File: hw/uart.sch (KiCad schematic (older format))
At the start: 10 parts

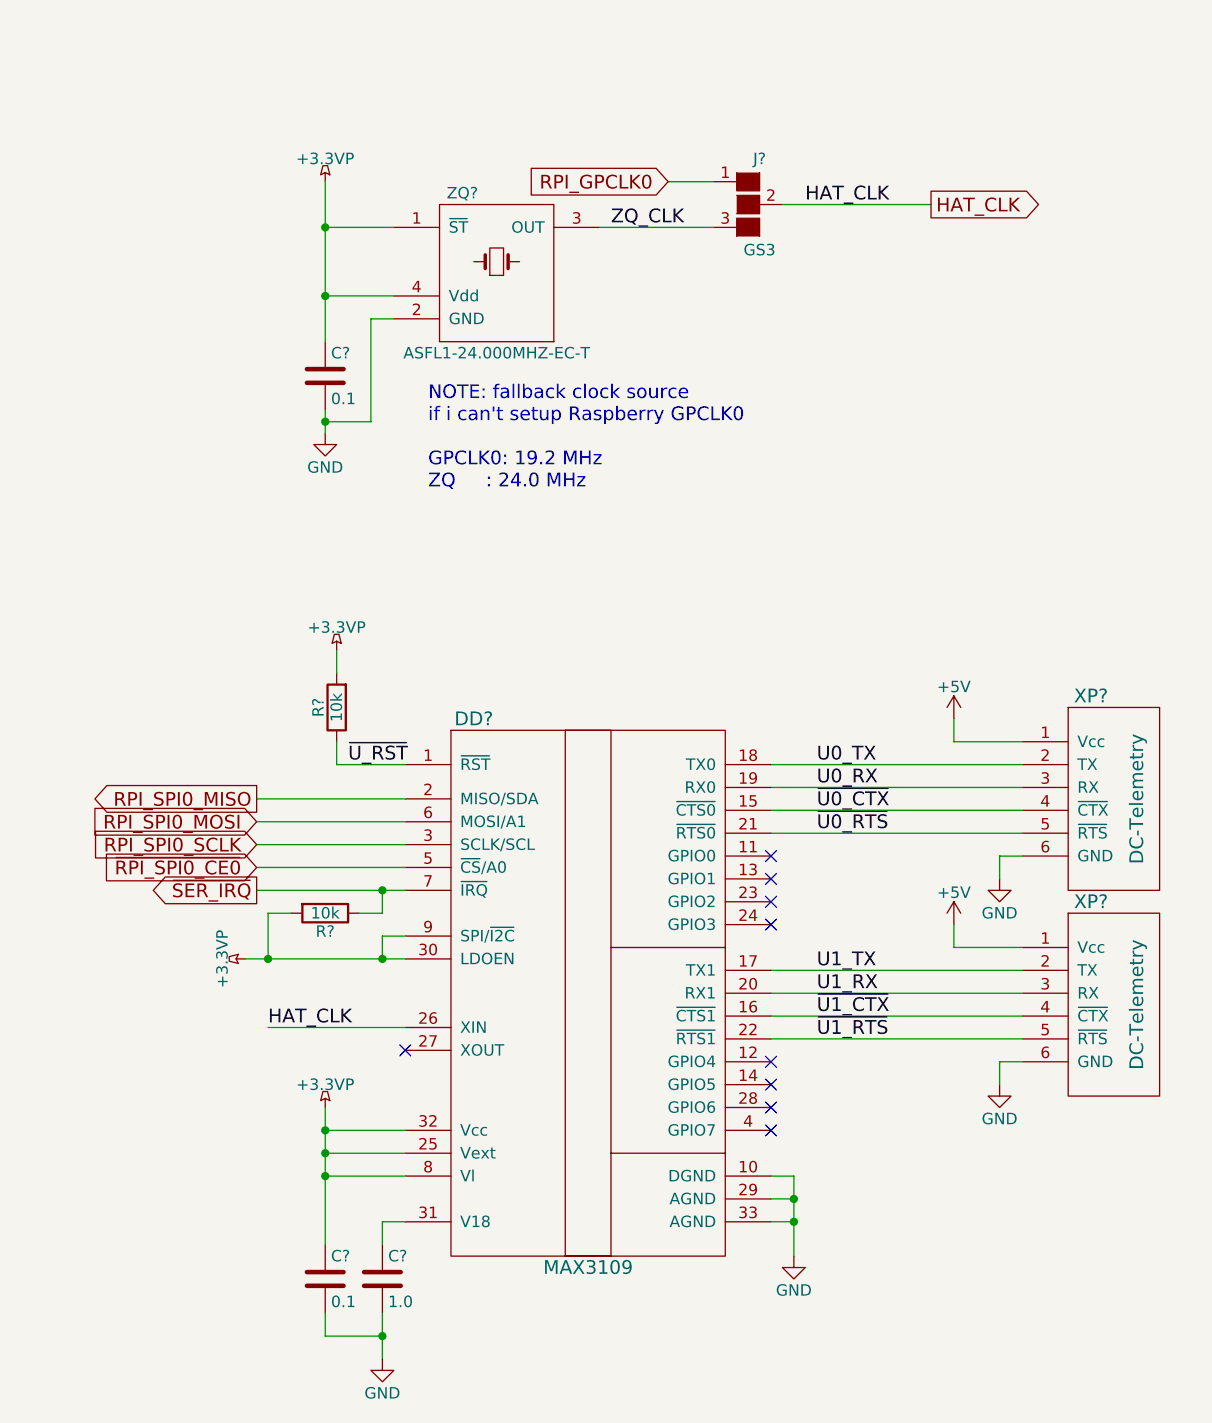
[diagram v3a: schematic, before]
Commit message: hw: add RTC sheet
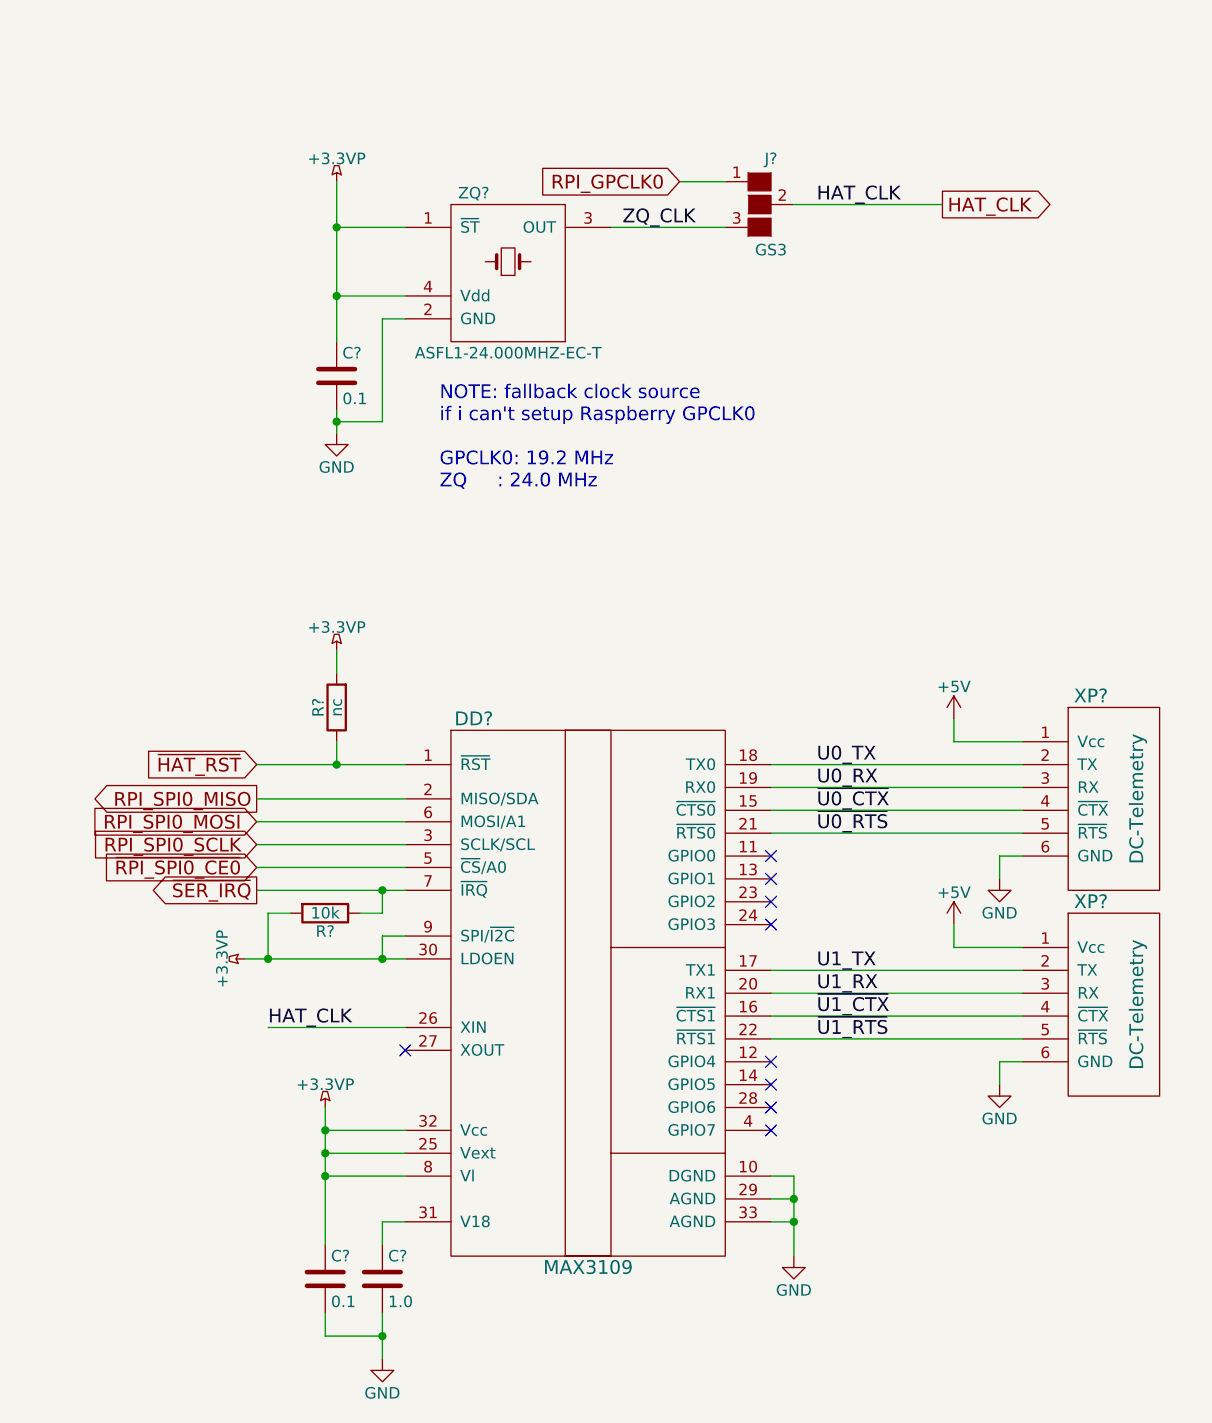
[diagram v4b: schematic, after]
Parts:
- R?: value 10k -> nc
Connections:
- net ~U_RST renamed ~HAT_RST
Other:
- moved on the sheet: C?, J?, ZQ?
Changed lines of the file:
@@
 P 3150 5350
 F 0 "R?" V 3230 5350 50  0000 C CNN
-F 1 "10k" V 3150 5350 50  0000 C CNN
+F 1 "nc" V 3150 5350 50  0000 C CNN
 F 2 "" V 3080 5350 50  0001 C CNN
 F 3 "" H 3150 5350 50  0001 C CNN
@@
 $EndComp
 Wire Wire Line
-	3450 5600 3150 5600
+	2800 5600 3450 5600
 Wire Wire Line
 	3150 5600 3150 5500
@@
 L ASFL1 ZQ?
 U 1 1 5AB33753
-P 3850 3400
-F 0 "ZQ?" H 3700 3700 50  0000 C CNN
-F 1 "ASFL1-24.000MHZ-EC-T" H 3850 3000 50  0000 C CNN
-F 2 "Crystals:Crystal_SMD_Abracon_ABM3B-4pin_5.0x3.2mm" H 3850 3400 50  0001 C CNN
-F 3 "https://www.terraelectronica.ru/pdf/show?pdf_file=%252Fds%252Fpdf%252FA%252FASFL1-24.pdf" H 3850 3400 50  0001 C CNN
-	1    3850 3400
+P 3900 3400
+F 0 "ZQ?" H 3750 3700 50  0000 C CNN
+F 1 "ASFL1-24.000MHZ-EC-T" H 3900 3000 50  0000 C CNN
+F 2 "Crystals:Crystal_SMD_Abracon_ABM3B-4pin_5.0x3.2mm" H 3900 3400 50  0001 C CNN
+F 3 "https://www.terraelectronica.ru/pdf/show?pdf_file=%252Fds%252Fpdf%252FA%252FASFL1-24.pdf" H 3900 3400 50  0001 C CNN
+	1    3900 3400
 	1    0    0    -1
 $EndComp
@@
 L +3.3VP #PWR?
 U 1 1 5AB34755
-P 3100 3050
-F 0 "#PWR?" H 3250 3000 50  0001 C CNN
-F 1 "+3.3VP" H 3100 3150 50  0000 C CNN
-F 2 "" H 3100 3050 50  0001 C CNN
-F 3 "" H 3100 3050 50  0001 C CNN
-	1    3100 3050
+P 3150 3050
+F 0 "#PWR?" H 3300 3000 50  0001 C CNN
+F 1 "+3.3VP" H 3150 3150 50  0000 C CNN
+F 2 "" H 3150 3050 50  0001 C CNN
+F 3 "" H 3150 3050 50  0001 C CNN
+	1    3150 3050
 	1    0    0    -1
 $EndComp
@@
 L C C?
 U 1 1 5AB3478D
-P 3100 3900
-F 0 "C?" H 3125 4000 50  0000 L CNN
-F 1 "0.1" H 3125 3800 50  0000 L CNN
-F 2 "" H 3138 3750 50  0001 C CNN
-F 3 "" H 3100 3900 50  0001 C CNN
-	1    3100 3900
+P 3150 3900
+F 0 "C?" H 3175 4000 50  0000 L CNN
+F 1 "0.1" H 3175 3800 50  0000 L CNN
+F 2 "" H 3188 3750 50  0001 C CNN
+F 3 "" H 3150 3900 50  0001 C CNN
+	1    3150 3900
 	1    0    0    -1
 $EndComp
@@
 L GND #PWR?
 U 1 1 5AB347BB
-P 3100 4150
-F 0 "#PWR?" H 3100 3900 50  0001 C CNN
-F 1 "GND" H 3100 4000 50  0000 C CNN
-F 2 "" H 3100 4150 50  0001 C CNN
-F 3 "" H 3100 4150 50  0001 C CNN
-	1    3100 4150
-	1    0    0    -1
-$EndComp
-Wire Wire Line
-	3100 3550 3400 3550
-Wire Wire Line
-	3100 3050 3100 3750
-Connection ~ 3100 3550
-Wire Wire Line
-	3100 4050 3100 4150
-Wire Wire Line
-	3400 3650 3300 3650
-Wire Wire Line
-	3300 3650 3300 4100
-Wire Wire Line
-	3300 4100 3100 4100
-Connection ~ 3100 4100
-Wire Wire Line
-	3400 3250 3100 3250
-Connection ~ 3100 3250
+P 3150 4150
+F 0 "#PWR?" H 3150 3900 50  0001 C CNN
+F 1 "GND" H 3150 4000 50  0000 C CNN
+F 2 "" H 3150 4150 50  0001 C CNN
+F 3 "" H 3150 4150 50  0001 C CNN
+	1    3150 4150
+	1    0    0    -1
+$EndComp
+Wire Wire Line
+	3150 3550 3450 3550
+Wire Wire Line
+	3150 3050 3150 3750
+Connection ~ 3150 3550
+Wire Wire Line
+	3150 4050 3150 4150
+Wire Wire Line
+	3450 3650 3350 3650
+Wire Wire Line
+	3350 3650 3350 4100
+Wire Wire Line
+	3350 4100 3150 4100
+Connection ~ 3150 4100
+Wire Wire Line
+	3450 3250 3150 3250
+Connection ~ 3150 3250
 $Comp
 L GS3 J?
 U 1 1 5AB34FDF
-P 4950 3150
-F 0 "J?" H 5000 3350 50  0000 C CNN
-F 1 "GS3" H 5000 2951 50  0000 C CNN
-F 2 "Connectors:GS3" V 5038 3076 50  0001 C CNN
-F 3 "" H 4950 3150 50  0001 C CNN
-	1    4950 3150
-	1    0    0    -1
-$EndComp
-Text GLabel 4600 3050 0    60   Input ~ 0
+P 5000 3150
+F 0 "J?" H 5050 3350 50  0000 C CNN
+F 1 "GS3" H 5050 2951 50  0000 C CNN
+F 2 "Connectors:GS3" V 5088 3076 50  0001 C CNN
+F 3 "" H 5000 3150 50  0001 C CNN
+	1    5000 3150
+	1    0    0    -1
+$EndComp
+Text GLabel 4650 3050 0    60   Input ~ 0
 RPI_GPCLK0
 Wire Wire Line
-	4800 3250 4300 3250
-Wire Wire Line
-	4600 3050 4800 3050
-Text Label 4350 3250 0    60   ~ 0
+	4850 3250 4350 3250
+Wire Wire Line
+	4650 3050 4850 3050
+Text Label 4400 3250 0    60   ~ 0
 ZQ_CLK
-Text GLabel 5750 3150 2    60   Output ~ 0
+Text GLabel 5800 3150 2    60   Output ~ 0
 HAT_CLK
 Wire Wire Line
-	5100 3150 5750 3150
-Text Label 5200 3150 0    60   ~ 0
+	5150 3150 5800 3150
+Text Label 5250 3150 0    60   ~ 0
 HAT_CLK
-Text Notes 3550 4400 0    60   ~ 0
+Text Notes 3600 4400 0    60   ~ 0
 NOTE: fallback clock source\nif i can't setup Raspberry GPCLK0\n\nGPCLK0: 19.2 MHz\nZQ     : 24.0 MHz
-Text Label 3200 5600 0    60   ~ 0
-~U_RST
 Wire Wire Line
 	3450 6750 2850 6750
@@
 NoConn ~ 5050 7100
 NoConn ~ 5050 7200
+Text GLabel 2800 5600 0    60   Input ~ 0
+~HAT_RST
+Connection ~ 3150 5600
 $EndSCHEMATC

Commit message: switch to KiCAD 5 (nightly)
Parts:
- removed C?: 0.1, symbol C
- removed C?: 1.0, symbol C
- removed J?: GS3, Connectors:GS3, symbol GS3
- added C? (x2): 0.1, symbol Device:C
- added JP?: Jumper_3_Open, symbol Jumper:Jumper_3_Open
- C?: symbol C -> Device:C
- DD?: symbol MAX3109 -> ic:MAX3109
- R? (x2): symbol R -> Device:R
- XP? (x2): symbol DC-Telemetry -> dronecode_con:DC-Telemetry
- ZQ?: symbol ASFL1 -> ic:ASFL1
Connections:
- net +3.3VP: now also C?.1
- net GND: now also C?.2, C?.2
- net HAT_CLK: now also JP?.2 (C)
- net RPI_GPCLK0: now also JP?.3 (B)
- net ZQ_CLK: now also JP?.1 (A)
- net at DD?.31 (V18): now also C?.1
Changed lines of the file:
@@
-EESchema Schematic File Version 2
-LIBS:power
-LIBS:device
-LIBS:transistors
-LIBS:conn
-LIBS:linear
-LIBS:regul
-LIBS:74xx
-LIBS:cmos4000
-LIBS:adc-dac
-LIBS:memory
-LIBS:xilinx
-LIBS:microcontrollers
-LIBS:dsp
-LIBS:microchip
-LIBS:analog_switches
-LIBS:motorola
-LIBS:texas
-LIBS:intel
-LIBS:audio
-LIBS:interface
-LIBS:digital-audio
-LIBS:philips
-LIBS:display
-LIBS:cypress
-LIBS:siliconi
-LIBS:opto
-LIBS:atmel
-LIBS:contrib
-LIBS:valves
-LIBS:rpi_con
-LIBS:ic
-LIBS:dronecode_con
+EESchema Schematic File Version 4
 LIBS:obc-drone-hat-cache
-EELAYER 25 0
+EELAYER 26 0
 EELAYER END
 $Descr A4 8268 11693 portrait
@@
 $EndDescr
 $Comp
-L MAX3109 DD?
+L ic:MAX3109 DD?
 U 1 1 5AB1B0A7
 P 4250 6600
@@
 $EndComp
 $Comp
-L +3.3VP #PWR013
+L power:+3.3VP #PWR013
 U 1 1 5AB1B260
 P 3100 7100
@@
 $EndComp
 $Comp
-L GND #PWR014
+L power:GND #PWR014
 U 1 1 5AB1B2D7
 P 3350 8200
@@
 $EndComp
 NoConn ~ 3450 6850
-$Comp
-L C C?
-U 1 1 5AB1B470
-P 3100 7850
-F 0 "C?" H 3125 7950 50  0000 L CNN
-F 1 "0.1" H 3125 7750 50  0000 L CNN
-F 2 "" H 3138 7700 50  0001 C CNN
-F 3 "" H 3100 7850 50  0001 C CNN
-	1    3100 7850
-	1    0    0    -1
-$EndComp
-$Comp
-L C C?
-U 1 1 5AB1B4D8
-P 3350 7850
-F 0 "C?" H 3375 7950 50  0000 L CNN
-F 1 "1.0" H 3375 7750 50  0000 L CNN
-F 2 "" H 3388 7700 50  0001 C CNN
-F 3 "" H 3350 7850 50  0001 C CNN
-	1    3350 7850
-	1    0    0    -1
-$EndComp
 Wire Wire Line
 	3450 7600 3350 7600
@@
 	3450 7200 3100 7200
 Wire Wire Line
-	3100 7100 3100 7700
+	3100 7100 3100 7200
 Wire Wire Line
 	3100 7300 3450 7300
@@
 Connection ~ 3100 7200
 Wire Wire Line
-	3350 8000 3350 8200
+	3350 8000 3350 8100
 Wire Wire Line
 	3350 8100 3100 8100
@@
 Connection ~ 3350 8100
 $Comp
-L +3.3VP #PWR015
+L power:+3.3VP #PWR015
 U 1 1 5AB1B914
 P 2750 6450
@@
 $EndComp
 $Comp
-L R R?
+L Device:R R?
 U 1 1 5AB1B9A3
 P 3100 6250
@@
 $EndComp
 Wire Wire Line
-	2750 6450 3450 6450
+	2750 6450 2850 6450
 Wire Wire Line
 	3450 6350 3350 6350
@@
 	3450 6050 2800 6050
 Wire Wire Line
-	2800 6150 3450 6150
+	2800 6150 3350 6150
 Wire Wire Line
 	3250 6250 3350 6250
@@
 Connection ~ 3350 6150
 $Comp
-L GND #PWR016
+L power:GND #PWR016
 U 1 1 5AB1C686
 P 6050 6100
@@
 	5050 7400 5150 7400
 Wire Wire Line
-	5150 7400 5150 7750
+	5150 7400 5150 7500
 Wire Wire Line
 	5050 7500 5150 7500
@@
 Connection ~ 5150 7600
 $Comp
-L R R?
+L Device:R R?
 U 1 1 5AB1D90A
 P 3150 5350
@@
 $EndComp
 $Comp
-L +3.3VP #PWR017
+L power:+3.3VP #PWR017
 U 1 1 5AB1D959
 P 3150 5100
@@
 $EndComp
 Wire Wire Line
-	2800 5600 3450 5600
+	2800 5600 3150 5600
 Wire Wire Line
 	3150 5600 3150 5500
@@
 	3150 5200 3150 5100
 $Comp
-L DC-Telemetry XP?
+L dronecode_con:DC-Telemetry XP?
 U 1 1 5AB2FA79
 P 6550 5750
@@
 $EndComp
 $Comp
-L DC-Telemetry XP?
+L dronecode_con:DC-Telemetry XP?
 U 1 1 5AB2FFF0
 P 6550 6650
@@
 	6150 6800 5050 6800
 $Comp
-L +5V #PWR?
+L power:+5V #PWR?
 U 1 1 5AB3063A
 P 5850 5400
@@
 	6050 6000 6050 6100
 $Comp
-L GND #PWR?
+L power:GND #PWR?
 U 1 1 5AB30BD8
 P 5150 7750
@@
 $EndComp
 $Comp
-L GND #PWR?
+L power:GND #PWR?
 U 1 1 5AB30BF8
 P 6050 7000
@@
 $EndComp
 $Comp
-L +5V #PWR?
+L power:+5V #PWR?
 U 1 1 5AB30E1E
 P 5850 6300
@@
 ~U1_RTS
 $Comp
-L ASFL1 ZQ?
+L ic:ASFL1 ZQ?
 U 1 1 5AB33753
 P 3900 3400
@@
 $EndComp
 $Comp
-L +3.3VP #PWR?
+L power:+3.3VP #PWR?
 U 1 1 5AB34755
 P 3150 3050
@@
 $EndComp
 $Comp
-L C C?
+L Device:C C?
 U 1 1 5AB3478D
 P 3150 3900
@@
 $EndComp
 $Comp
-L GND #PWR?
+L power:GND #PWR?
 U 1 1 5AB347BB
 P 3150 4150
@@
 	3150 3550 3450 3550
 Wire Wire Line
-	3150 3050 3150 3750
+	3150 3050 3150 3250
 Connection ~ 3150 3550
 Wire Wire Line
-	3150 4050 3150 4150
+	3150 4050 3150 4100
 Wire Wire Line
 	3450 3650 3350 3650
@@
 	3450 3250 3150 3250
 Connection ~ 3150 3250
-$Comp
-L GS3 J?
-U 1 1 5AB34FDF
-P 5000 3150
-F 0 "J?" H 5050 3350 50  0000 C CNN
-F 1 "GS3" H 5050 2951 50  0000 C CNN
-F 2 "Connectors:GS3" V 5088 3076 50  0001 C CNN
-F 3 "" H 5000 3150 50  0001 C CNN
-	1    5000 3150
-	1    0    0    -1
-$EndComp
-Text GLabel 4650 3050 0    60   Input ~ 0
+Text GLabel 4800 2400 0    60   Input ~ 0
 RPI_GPCLK0
 Wire Wire Line
-	4850 3250 4350 3250
-Wire Wire Line
-	4650 3050 4850 3050
+	5200 3250 4350 3250
+Wire Wire Line
+	4800 2400 5200 2400
 Text Label 4400 3250 0    60   ~ 0
 ZQ_CLK
-Text GLabel 5800 3150 2    60   Output ~ 0
+Text GLabel 5950 2800 2    60   Output ~ 0
 HAT_CLK
 Wire Wire Line
-	5150 3150 5800 3150
-Text Label 5250 3150 0    60   ~ 0
+	5350 2800 5950 2800
+Text Label 5400 2800 0    60   ~ 0
 HAT_CLK
 Text Notes 3600 4400 0    60   ~ 0
@@
 ~HAT_RST
 Connection ~ 3150 5600
+Wire Wire Line
+	3100 7300 3100 7400
+Wire Wire Line
+	3100 7400 3100 7700
+Wire Wire Line
+	3100 7200 3100 7300
+Wire Wire Line
+	3350 8100 3350 8200
+Wire Wire Line
+	3350 6450 3450 6450
+Wire Wire Line
+	2850 6450 3350 6450
+Wire Wire Line
+	3350 6150 3450 6150
+Wire Wire Line
+	5150 7500 5150 7600
+Wire Wire Line
+	5150 7600 5150 7750
+Wire Wire Line
+	3150 3550 3150 3750
+Wire Wire Line
+	3150 4100 3150 4150
+Wire Wire Line
+	3150 3250 3150 3550
+Wire Wire Line
+	3150 5600 3450 5600
+$Comp
+L Jumper:Jumper_3_Open JP?
+U 1 1 5AB6CF92
+P 5200 2800
+F 0 "JP?" V 5246 2886 50  0000 L CNN
+F 1 "Jumper_3_Open" V 5155 2886 50  0000 L CNN
+F 2 "" H 5200 2800 50  0001 C CNN
+F 3 "~" H 5200 2800 50  0001 C CNN
+	1    5200 2800
+	0    -1   -1   0
+$EndComp
+Wire Wire Line
+	5200 2400 5200 2550
+Wire Wire Line
+	5200 3250 5200 3050
+$Comp
+L Device:C C?
+U 1 1 5AC0F665
+P 3100 7850
+F 0 "C?" H 2700 8050 50  0000 L CNN
+F 1 "0.1" H 2850 8050 50  0000 L CNN
+F 2 "" H 3138 7700 50  0001 C CNN
+F 3 "~" H 3100 7850 50  0001 C CNN
+	1    3100 7850
+	1    0    0    -1
+$EndComp
+$Comp
+L Device:C C?
+U 1 1 5AC0F72E
+P 3350 7850
+F 0 "C?" H 2700 7950 50  0000 L CNN
+F 1 "0.1" H 2850 7950 50  0000 L CNN
+F 2 "" H 3388 7700 50  0001 C CNN
+F 3 "~" H 3350 7850 50  0001 C CNN
+	1    3350 7850
+	1    0    0    -1
+$EndComp
 $EndSCHEMATC

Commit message: hw: start stm page
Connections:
- net +3.3VP renamed +3V3
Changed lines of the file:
@@
-$EndComp
-$Comp
-L power:+3.3VP #PWR013
-U 1 1 5AB1B260
-P 3100 7100
-F 0 "#PWR013" H 3250 7050 50  0001 C CNN
-F 1 "+3.3VP" H 3100 7200 50  0000 C CNN
-F 2 "" H 3100 7100 50  0001 C CNN
-F 3 "" H 3100 7100 50  0001 C CNN
-	1    3100 7100
-	1    0    0    -1
 $EndComp
 $Comp
@@
 	3100 8100 3100 8000
 Connection ~ 3350 8100
-$Comp
-L power:+3.3VP #PWR015
-U 1 1 5AB1B914
-P 2750 6450
-F 0 "#PWR015" H 2900 6400 50  0001 C CNN
-F 1 "+3.3VP" H 2750 6550 50  0000 C CNN
-F 2 "" H 2750 6450 50  0001 C CNN
-F 3 "" H 2750 6450 50  0001 C CNN
-	1    2750 6450
-	0    -1   -1   0
-$EndComp
 $Comp
 L Device:R R?
@@
 	1    3150 5350
 	-1   0    0    1
-$EndComp
-$Comp
-L power:+3.3VP #PWR017
-U 1 1 5AB1D959
-P 3150 5100
-F 0 "#PWR017" H 3300 5050 50  0001 C CNN
-F 1 "+3.3VP" H 3150 5200 50  0000 C CNN
-F 2 "" H 3150 5100 50  0001 C CNN
-F 3 "" H 3150 5100 50  0001 C CNN
-	1    3150 5100
-	1    0    0    -1
 $EndComp
 Wire Wire Line
@@
 $EndComp
 $Comp
-L power:+3.3VP #PWR?
-U 1 1 5AB34755
-P 3150 3050
-F 0 "#PWR?" H 3300 3000 50  0001 C CNN
-F 1 "+3.3VP" H 3150 3150 50  0000 C CNN
-F 2 "" H 3150 3050 50  0001 C CNN
-F 3 "" H 3150 3050 50  0001 C CNN
-	1    3150 3050
-	1    0    0    -1
-$EndComp
-$Comp
 L Device:C C?
 U 1 1 5AB3478D
@@
 L power:GND #PWR?
 U 1 1 5AB347BB
-P 3150 4150
-F 0 "#PWR?" H 3150 3900 50  0001 C CNN
-F 1 "GND" H 3150 4000 50  0000 C CNN
-F 2 "" H 3150 4150 50  0001 C CNN
-F 3 "" H 3150 4150 50  0001 C CNN
-	1    3150 4150
+P 3150 4250
+F 0 "#PWR?" H 3150 4000 50  0001 C CNN
+F 1 "GND" H 3150 4100 50  0000 C CNN
+F 2 "" H 3150 4250 50  0001 C CNN
+F 3 "" H 3150 4250 50  0001 C CNN
+	1    3150 4250
 	1    0    0    -1
 $EndComp
@@
 Connection ~ 3150 3550
 Wire Wire Line
-	3150 4050 3150 4100
+	3150 4050 3150 4150
 Wire Wire Line
 	3450 3650 3350 3650
 Wire Wire Line
-	3350 3650 3350 4100
-Wire Wire Line
-	3350 4100 3150 4100
-Connection ~ 3150 4100
+	3350 3650 3350 4150
+Wire Wire Line
+	3350 4150 3150 4150
+Connection ~ 3150 4150
 Wire Wire Line
 	3450 3250 3150 3250
@@
 	3150 3550 3150 3750
 Wire Wire Line
-	3150 4100 3150 4150
+	3150 4150 3150 4250
 Wire Wire Line
 	3150 3250 3150 3550
@@
 	1    0    0    -1
 $EndComp
+$Comp
+L power:+3.3V #PWR?
+U 1 1 5AC2B996
+P 3150 3050
+F 0 "#PWR?" H 3150 2900 50  0001 C CNN
+F 1 "+3.3V" H 3165 3223 50  0000 C CNN
+F 2 "" H 3150 3050 50  0001 C CNN
+F 3 "" H 3150 3050 50  0001 C CNN
+	1    3150 3050
+	1    0    0    -1
+$EndComp
+$Comp
+L power:+3.3V #PWR?
+U 1 1 5AC2B9D6
+P 3150 5100
+F 0 "#PWR?" H 3150 4950 50  0001 C CNN
+F 1 "+3.3V" H 3165 5273 50  0000 C CNN
+F 2 "" H 3150 5100 50  0001 C CNN
+F 3 "" H 3150 5100 50  0001 C CNN
+	1    3150 5100
+	1    0    0    -1
+$EndComp
+$Comp
+L power:+3.3V #PWR?
+U 1 1 5AC2BA1D
+P 2750 6450
+F 0 "#PWR?" H 2750 6300 50  0001 C CNN
+F 1 "+3.3V" V 2765 6578 50  0000 L CNN
+F 2 "" H 2750 6450 50  0001 C CNN
+F 3 "" H 2750 6450 50  0001 C CNN
+	1    2750 6450
+	0    -1   -1   0
+$EndComp
+$Comp
+L power:+3.3V #PWR?
+U 1 1 5AC2C6EA
+P 3100 7100
+F 0 "#PWR?" H 3100 6950 50  0001 C CNN
+F 1 "+3.3V" H 3115 7273 50  0000 C CNN
+F 2 "" H 3100 7100 50  0001 C CNN
+F 3 "" H 3100 7100 50  0001 C CNN
+	1    3100 7100
+	1    0    0    -1
+$EndComp

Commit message: hw: update libs
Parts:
- DD?: symbol ic:MAX3109 -> hat-ic:MAX3109
- XP? (x2): symbol dronecode_con:DC-Telemetry -> dronecode-conn:DC-Telemetry
- ZQ?: symbol ic:ASFL1 -> hat-ic:ASFL1
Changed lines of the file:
@@
 $EndDescr
 $Comp
-L ic:MAX3109 DD?
+L hat-ic:MAX3109 DD?
 U 1 1 5AB1B0A7
 P 4250 6600
@@
 	3150 5200 3150 5100
 $Comp
-L dronecode_con:DC-Telemetry XP?
+L dronecode-conn:DC-Telemetry XP?
 U 1 1 5AB2FA79
 P 6550 5750
@@
 $EndComp
 $Comp
-L dronecode_con:DC-Telemetry XP?
+L dronecode-conn:DC-Telemetry XP?
 U 1 1 5AB2FFF0
 P 6550 6650
@@
 ~U1_RTS
 $Comp
-L ic:ASFL1 ZQ?
+L hat-ic:ASFL1 ZQ?
 U 1 1 5AB33753
 P 3900 3400
